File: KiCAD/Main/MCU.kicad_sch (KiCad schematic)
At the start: 27 parts, among them J6 Conn_01x03, Q4 2N7002, SW1 RESET, SW2 USER, U4 STM32H750VBTx, Y2 SiT8008xx-2x-xxE (25MHz)

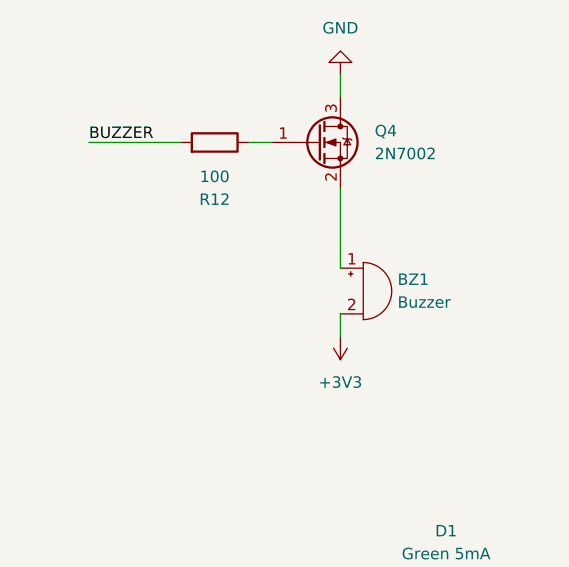
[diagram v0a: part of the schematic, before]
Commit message: Edit PCB Layout to increase min hole size and decrease price, prepare production files, prepare for main branch merge
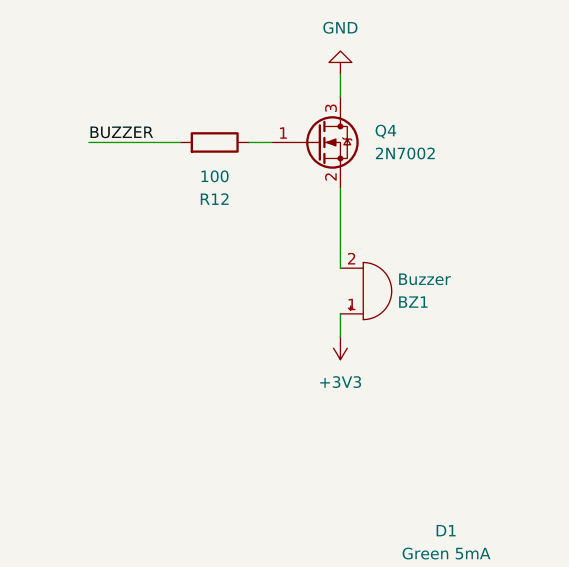
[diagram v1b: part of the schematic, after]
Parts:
- BZ1: footprint Buzzer_Beeper:MagneticBuzzer_PUI_SMT-1028-T-2-R -> Buzzer_Beeper:Buzzer_12x9.5RM7.6
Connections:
- net +3V3: now also BZ1.1 (+); no longer BZ1.2 (-)
- net at Q4.2 (S): now also BZ1.2 (-); no longer BZ1.1 (+)
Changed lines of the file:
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@@
 		(lib_id "Device:Buzzer")
 		(at 261.62 80.01 0)
+		(mirror x)
 		(unit 1)
 		(exclude_from_sim no)
@@
 		(on_board yes)
 		(dnp no)
-		(fields_autoplaced yes)
 		(property "Reference" "BZ1"
+			(at 265.43 81.28 0)
+			(effects
+				(font
+					(size 1.27 1.27)
+				)
+				(justify left)
+			)
+		)
+		(property "Value" "Buzzer"
 			(at 265.43 78.74 0)
 			(effects
@@
 			)
 		)
-		(property "Value" "Buzzer"
-			(at 265.43 81.28 0)
-			(effects
-				(font
-					(size 1.27 1.27)
-				)
-				(justify left)
-			)
-		)
-		(property "Footprint" "Buzzer_Beeper:MagneticBuzzer_PUI_SMT-1028-T-2-R"
-			(at 260.985 77.47 90)
+		(property "Footprint" "Buzzer_Beeper:Buzzer_12x9.5RM7.6"
+			(at 260.985 82.55 90)
 			(effects
 				(font
@@
 		)
 		(property "Datasheet" "~"
-			(at 260.985 77.47 90)
+			(at 260.985 82.55 90)
 			(effects
 				(font
